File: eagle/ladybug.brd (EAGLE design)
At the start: 36 x 30 mm, 11 parts

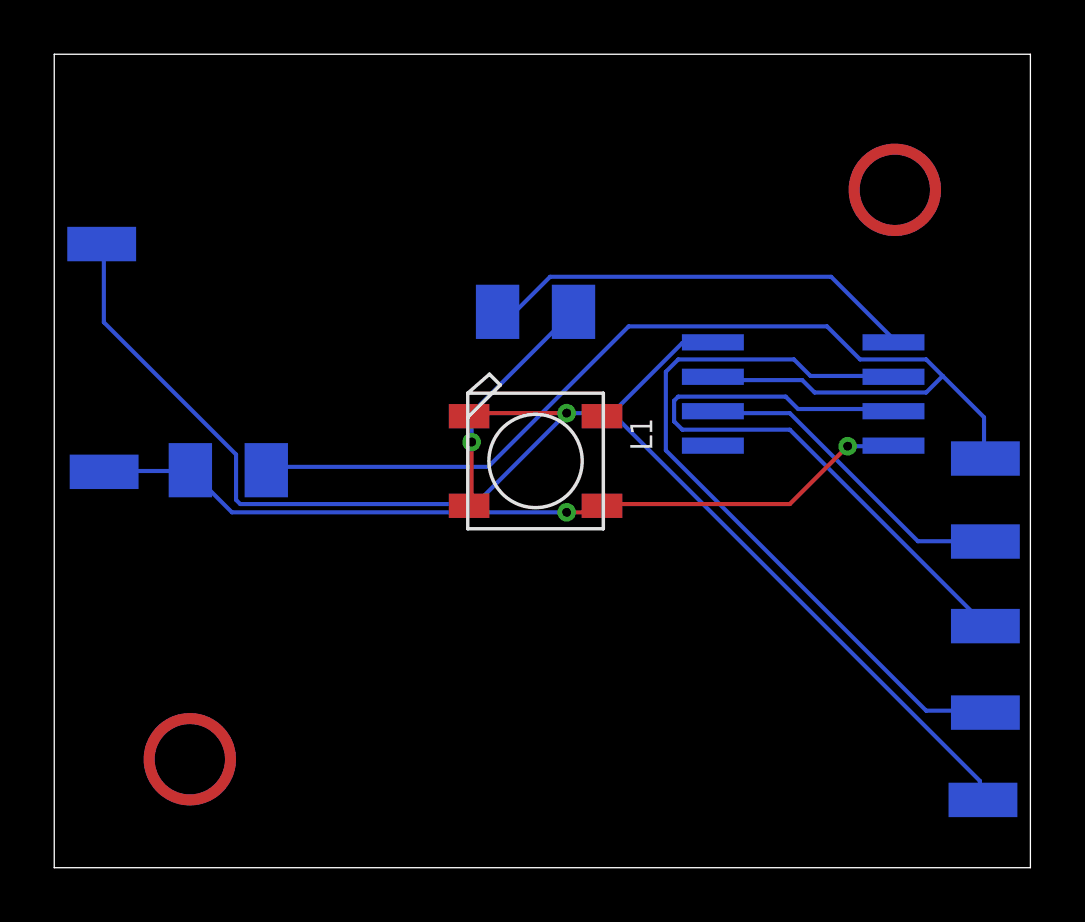
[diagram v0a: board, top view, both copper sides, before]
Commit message: Fixed ground plane and drill holes.
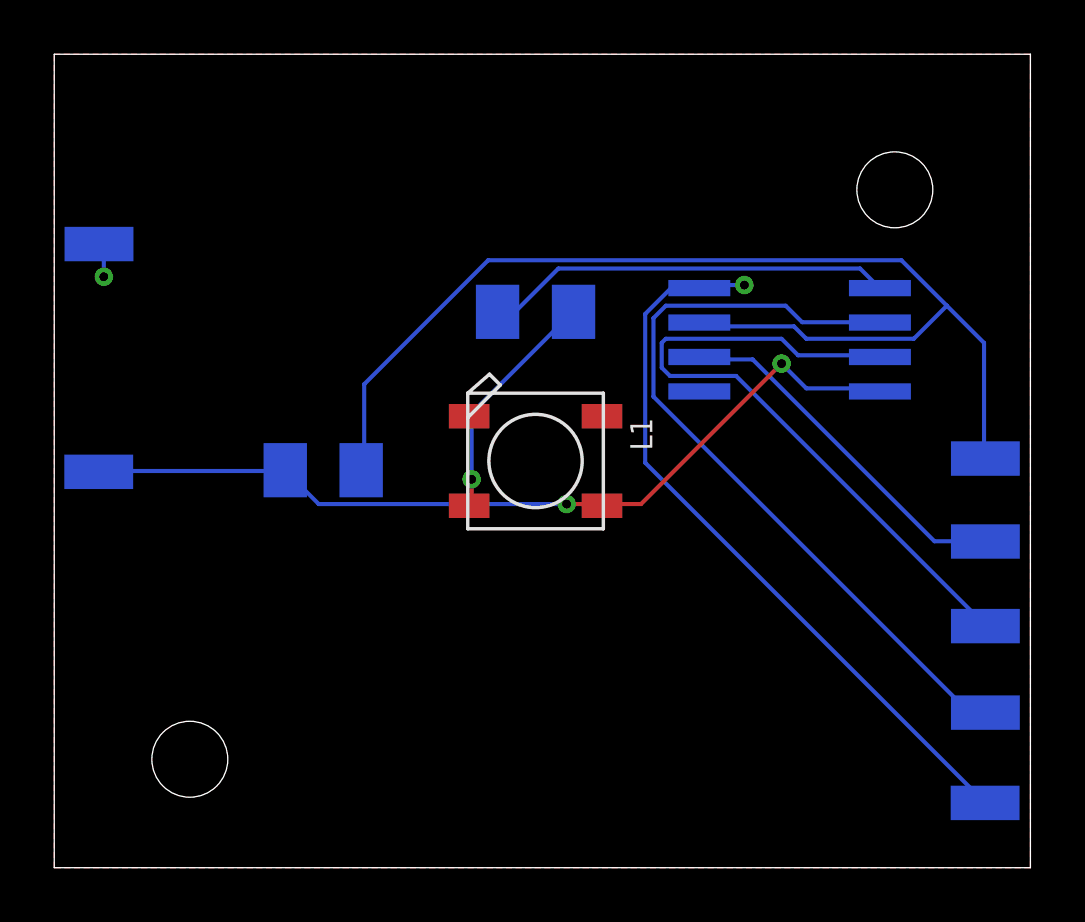
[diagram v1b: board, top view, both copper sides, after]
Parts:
- moved R1 3.50 mm to (9.92, 14.7)
- moved U1 2.06 mm to (27.1, 19.5)
- moved VCC 0.20 mm to (1.64, 14.6)
- moved GND 0.14 mm to (34.3, 2.39)
- moved VSS 0.10 mm to (1.65, 23.0)
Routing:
- net VSS: track 55.2 -> 28.6 mm, vias 1 -> 2
- net PB3: track 40.6 -> 43.4 mm
- net N$5: track 23.8 -> 25.2 mm
- net N$3: track 12.0 -> 13.4 mm
- net N$4: track 27.6 -> 28.8 mm
- net VCC: track 30.8 -> 32.0 mm
- net N$1: track 16.2 -> 15.1 mm
- added copper zone on layer 1, net VSS
